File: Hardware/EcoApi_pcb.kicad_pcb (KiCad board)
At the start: 4 copper layers, 90.6 x 58 mm, 177 parts, among them IC1 PCF8563T_5,518, IC2 SIP32431DR3-T1GE3, IC3 SIP32431DR3-T1GE3, J1 UFL, J10 TILT, J12 POWER ON, J2 614105150721, J3 B2B-XH-A, J4 POWER ON, J5 DBG, J6 TRACE, J7 I2C INTERNAL, J8 B5B-XH-A__LF__SN_, J9 B8B-XH-A_LF__SN_, Q1 MMBT4403*, Q2 FDC638P, Q3 IRLML6244TRPBF, Q4 BSS138, Q5 BSS138, Q6 IRLML6244TRPBF, Q7 FDC638P, U1 TPL5010DDCR, U10 TPS63900DSKR, U13 STM32F411CEU6, U2 HX711, U4 MB85RC16PNF-G-JNE1, U5 RFM95W-868S2, U6 W25Q32JVSS, U7 24LC02B_SN, U8 TP4056, Y1 Crystal_Small, Y2 Crystal_Small, Y3 Crystal_GND24

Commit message: Fix drc error
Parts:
- added R58: 10K, Resistor_SMD:R_0603_1608Metric, B.Cu at (183.1, 84.0)
- F1, F2: footprint EcoApi_pcb:0603-F1608X100N -> EcoApi_pcb:FUSC1608X100N
- U10: footprint EcoApi_pcb:TPS63900DSKR -> EcoApi_pcb:SON50P250X250X80-11N-D
- moved C32 8.53 mm to (163.0, 74.2)
- moved R71 8.47 mm to (171.2, 74.1), turned to 180 degrees
- moved C34 1.32 mm to (189.3, 59.6), turned to 270 degrees
- moved R63 1.00 mm to (175.3, 74.1)
- moved C33 0.65 mm to (192.6, 58.6), turned to 0 degrees
- moved L2 0.61 mm to (162.4, 57.9)
- moved D7 0.58 mm to (181.8, 75.4), turned to 0 degrees
- moved C11 0.54 mm to (215.0, 47.7)
- moved L3 0.45 mm to (181.8, 60.1)
- moved C12 0.44 mm to (215.1, 49.4)
- moved C10 0.43 mm to (211.5, 49.4)
- moved R75 0.33 mm to (184.9, 60.2), turned to 90 degrees
- moved C42 0.32 mm to (180.2, 48.8)
- moved R74 0.32 mm to (186.1, 58.9)
- moved C36 0.20 mm to (186.2, 59.9)
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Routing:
- net NRST: track 75.0 -> 106.5 mm, vias 6 -> 4
- net GND: track 63.5 -> 77.3 mm, vias 47 -> 59
- net WDG_RELOAD: track 62.8 -> 74.8 mm
- net +3V3: track 325.6 -> 334.5 mm
- net WAKEUP: track 41.4 -> 47.3 mm
- net BOOT0: track 41.2 -> 46.5 mm
- net EN_AVBATT-BTN_TARE: track 49.5 -> 44.6 mm
- net +3V3_int: track 194.2 -> 190.3 mm
- net VBAT: track 259.8 -> 257.2 mm
- net Net-(C2-Pad1): track 6.23 -> 8.09 mm
- net Net-(R74-Pad2): track 5.56 -> 4.62 mm
- net Net-(C33-Pad1): track 11.0 -> 10.1 mm
- net WDG_ALARM: track 46.9 -> 46.1 mm
- net VREF+: track 4.20 -> 4.80 mm
- net Net-(L2-Pad2): track 2.67 -> 3.25 mm
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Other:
- board text added: "+"
- board text added: "3v3"
- board text added: "A+"
- board text added: "A-"
- board text added: "BOOT0 en LED info en TRACE en SCALE type (full - half) WDG delay 1 en WDG delay 2 en"
- board text added: "CHRG"
- board text added: "CK-GAIN"
- board text added: "CLK"
- board text added: "DIO"
- board text added: "DONE"
- board text added: "E+"
- board text added: "E-"
- board text added: "EcoApi V2.0 03/22"
- board text added: "GND"
- board text added: "INFO"
- board text added: "PWR en"
- board text added: "PWR on"
- board text added: "RESET"
- board text added: "RST"
- board text added: "RX"
- board text added: "SCL"
- board text added: "SD-ANA"
- board text added: "SDA"
- board text added: "SH"
- board text added: "TARE"
- board text added: "TX"
- board text added: "WS"

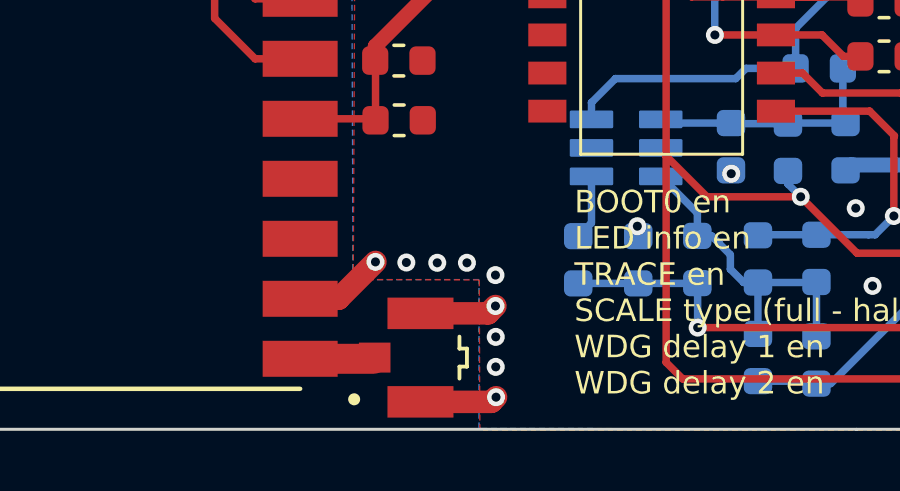
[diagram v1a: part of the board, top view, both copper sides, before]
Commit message: Add text on pcb front side
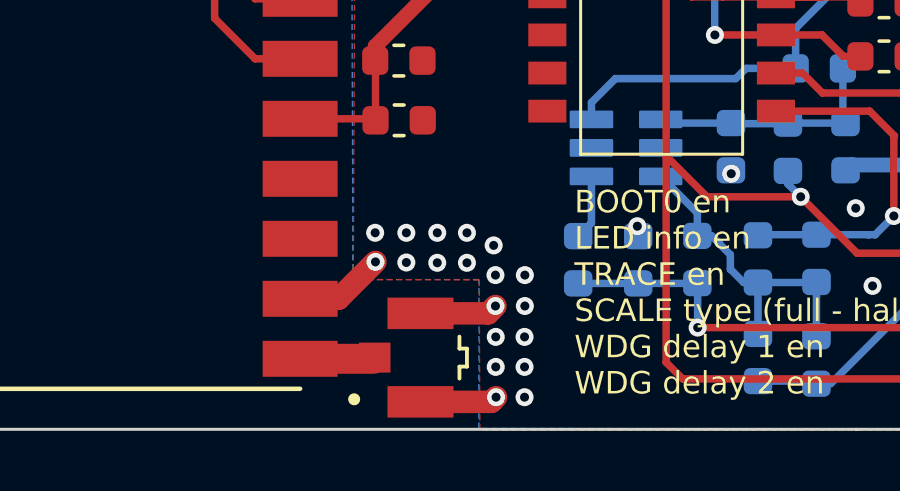
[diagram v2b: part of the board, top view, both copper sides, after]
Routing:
- net GND: vias 59 -> 69
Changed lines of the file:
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@@
     (thickness 1.6)
     (drawings 46)
-    (tracks 1760)
+    (tracks 1770)
     (zones 0)
     (modules 178)
@@
   )
   (setup
-    (last_trace_width 0.5)
+    (last_trace_width 0.25)
     (user_trace_width 0.4)
     (user_trace_width 0.5)
@@
   (gr_line (start 184.3 96) (end 220.6 96) (layer Edge.Cuts) (width 0.1))
   (gr_line (start 184.3 96) (end 148 96) (layer Edge.Cuts) (width 0.1))
-  (via (at 163.15 53.66) (size 0.6) (drill 0.3) (layers F.Cu B.Cu) (net 114))
-  (via (at 161.65 53.66) (size 0.6) (drill 0.3) (layers F.Cu B.Cu) (net 114))
-  (via (at 162.4 53.66) (size 0.6) (drill 0.3) (layers F.Cu B.Cu) (net 114))
   (segment (start 167.96 44.97) (end 167.96 40.6) (width 0.75) (layer F.Cu) (net 1))
   (segment (start 157.73 55.2) (end 167.96 44.97) (width 0.75) (layer F.Cu) (net 1))
@@
   (segment (start 205.94 52.23) (end 206.57 51.6) (width 0.5) (layer PWR) (net 113))
   (segment (start 205.94 53.19) (end 205.94 52.23) (width 0.5) (layer PWR) (net 113))
+  (via (at 163.15 53.66) (size 0.6) (drill 0.3) (layers F.Cu B.Cu) (net 114))
+  (via (at 161.65 53.66) (size 0.6) (drill 0.3) (layers F.Cu B.Cu) (net 114))
+  (via (at 162.4 53.66) (size 0.6) (drill 0.3) (layers F.Cu B.Cu) (net 114))
   (via (at 176.99 89.23) (size 0.6) (drill 0.3) (layers F.Cu B.Cu) (net 114))
   (via (at 180.12 87.48) (size 0.6) (drill 0.3) (layers F.Cu B.Cu) (net 114))
@@
   (via (at 181.65 77.1) (size 0.6) (drill 0.3) (layers F.Cu B.Cu) (net 114))
   (via (at 181.73 74.34) (size 0.6) (drill 0.3) (layers F.Cu B.Cu) (net 114))
+  (via (at 173.23 94.93) (size 0.6) (drill 0.3) (layers F.Cu B.Cu) (net 114))
+  (via (at 173.23 93.92) (size 0.6) (drill 0.3) (layers F.Cu B.Cu) (net 114))
+  (via (at 173.23 92.92) (size 0.6) (drill 0.3) (layers F.Cu B.Cu) (net 114))
+  (via (at 173.24 91.89) (size 0.6) (drill 0.3) (layers F.Cu B.Cu) (net 114))
+  (via (at 173.24 90.86) (size 0.6) (drill 0.3) (layers F.Cu B.Cu) (net 114))
+  (via (at 171.31 89.45) (size 0.6) (drill 0.3) (layers F.Cu B.Cu) (net 114))
+  (via (at 170.32 89.45) (size 0.6) (drill 0.3) (layers F.Cu B.Cu) (net 114))
+  (via (at 169.29 89.45) (size 0.6) (drill 0.3) (layers F.Cu B.Cu) (net 114))
+  (via (at 168.25 89.45) (size 0.6) (drill 0.3) (layers F.Cu B.Cu) (net 114))
+  (via (at 172.2 89.87) (size 0.6) (drill 0.3) (layers F.Cu B.Cu) (net 114))
   (zone (net 114) (net_name GND) (layer B.Cu) (hatch edge 0.508)
     (connect_pads yes (clearance 0.254))

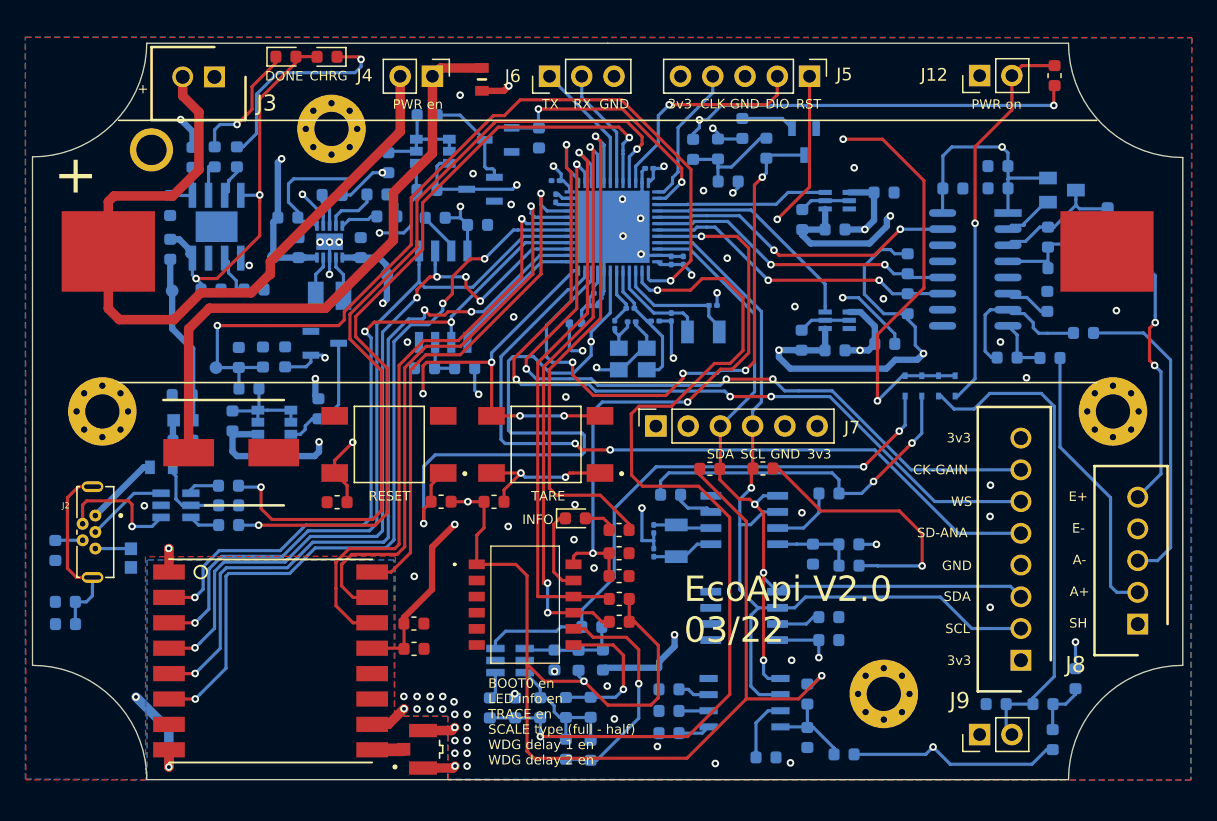
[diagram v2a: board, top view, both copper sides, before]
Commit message: Update pcb to v2.1 (Add ldo)
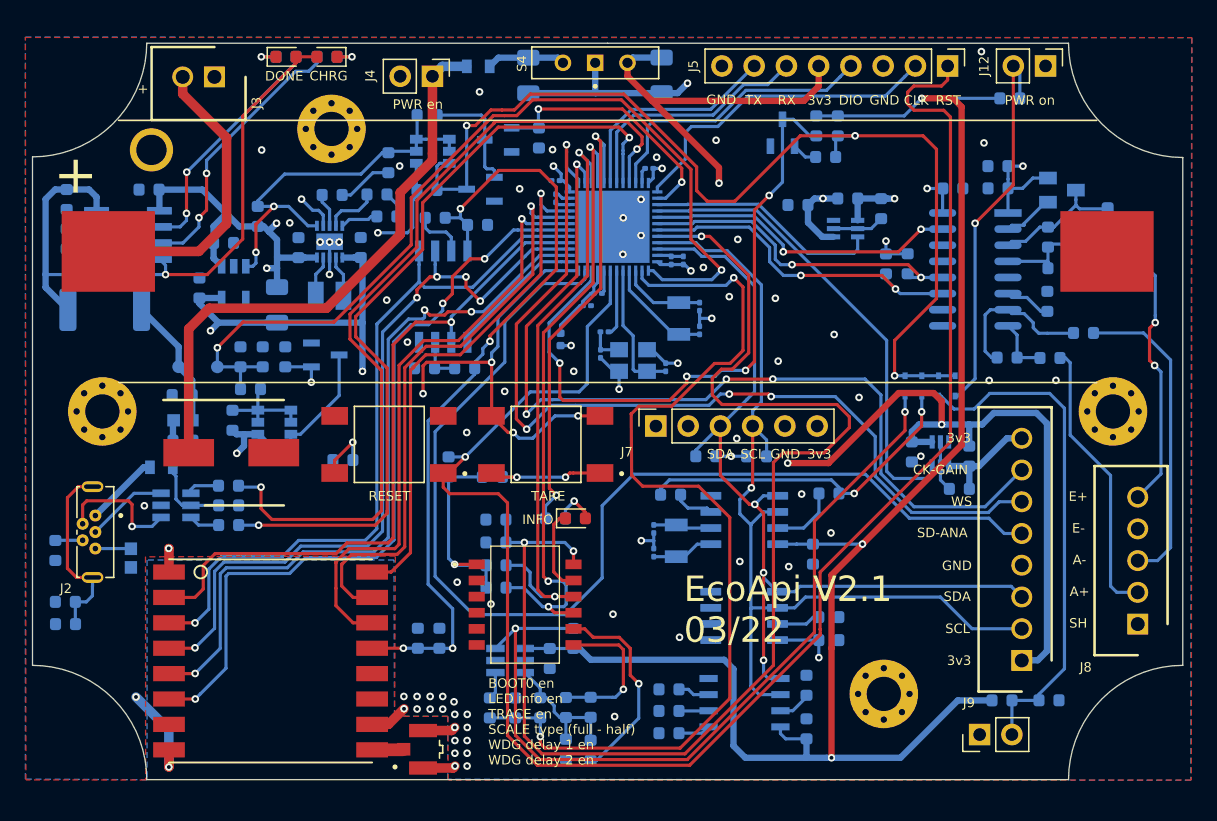
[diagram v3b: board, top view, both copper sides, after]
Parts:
- removed J6: TRACE, Connector_PinHeader_2.54mm:PinHeader_1x03_P2.54mm_Vertical
- removed R14, R43, R60, R64, R66: 0R, Resistor_SMD:R_0603_1608Metric
- removed R57: 100K, Resistor_SMD:R_0603_1608Metric
- removed R61, R62: 1M, Resistor_SMD:R_0603_1608Metric
- removed R74: 1M, Resistor_SMD:R_0201_0603Metric
- removed TP21, TP26, TP28: TestPoint, TestPoint:TestPoint_Pad_D1.0mm
- added C45: 1uF, Capacitor_SMD:C_0603_1608Metric, B.Cu at (152.2, 57.3)
- added C46: 10nF, Capacitor_SMD:C_0603_1608Metric, B.Cu at (157.1, 62.7)
- added PS1: NCP161ASN330T1G, EcoApi_pcb:SOT95P280X145-5N, B.Cu at (154.8, 56.8)
- added S4: MSS-102559-14A-D, EcoApi_pcb:SW_MSS-102559-14A-D, F.Cu at (183.3, 39.5)
- added TP3: TestPoint, TestPoint:TestPoint_Pad_D1.0mm, B.Cu at (153.6, 63.5)
- C10: value 0.1uF 0402 6.3V -> 0.1uF
- C11: value 0.1uF 0402 -> 0.1uF
- C12: value 10uF 0402 -> 10uF
- C13, C14, C15: value 100n -> 0.1uF
- C18: value EEE-FK0J102GP -> 1000uF
- C22, C30: value 100nF -> 0.1uF
- C23: value 10uF 6.3V X5R -> 10uF
- C24: value 22uF 6.3V x5R -> 22uF
- C26, C28: value 1u -> 1uF
- C27: value 0.01uF -> 1uF
- C29, C44: value 0.1u -> 0.1uF
- C31, C32: value 100nF -> 0.1uF; moved to B.Cu
- C35, C36: value 10u -> 10uF
- C4: value 10uF 0402 6.3V -> 10uF
- C5, C6, C7: value 100nF 0402 -> 0.1uF
- C8: value 100n -> 0.1uF; moved to B.Cu
- C9: value 10u -> 10uF; moved to B.Cu
- D1: value LED_0603_RED -> RED
- D2: value LED_0603_GREEN -> GREEN
- D7: value LED_0603_BLUE -> BLUE
- F2, R63, R72: moved to B.Cu
- J5: value DBG -> Debug; footprint Connector_PinHeader_2.54mm:PinHeader_1x05_P2.54mm_Vertical -> Connector_PinHeader_2.54mm:PinHeader_1x08_P2.54mm_Vertical
- L1, L3: value 3.3uH_0603 -> 3.3uH
- L2: value DFE252012P-2R2M=P2 -> 2.2uH
- Q1: value MMBT4403* -> MMBT4403
- R10, R46: footprint Resistor_SMD:R_0603_1608Metric -> Resistor_SMD:R_1206_3216Metric
- R15, R42, R45: value 0R -> 1M
- R21: value 22k -> 22K
- R22: value 20k -> 20K
- R23: value 0R -> 100K
- R26, R28: value 4.7k -> 4.7K; moved to B.Cu
- R29, R32: value 4.7k -> 4.7K
- R35: value 0.5R_2W_2512 -> 0.5R; footprint Resistor_SMD:R_0603_1608Metric -> Resistor_SMD:R_2512_6332Metric
- R52: value 36k5 -> 36.5K
- R56: value 1M -> 0R; footprint Resistor_SMD:R_0603_1608Metric -> Resistor_SMD:R_1206_3216Metric
- R67, R68, R69, R71, R73: value 10k -> 10K; moved to B.Cu
- U4: value MB85RC16PNF-G-JNE1 -> MB85RC04VPNF-G-JNERE1
- U7: value 24LC02B_SN -> 24LC02BT-I/SN
- moved R11 54.1 mm to (156.7, 51.6), turned to 270 degrees
- moved R23 54.0 mm to (158.9, 62.7), turned to 90 degrees
- moved R25 50.2 mm to (154.8, 67.7), turned to 90 degrees
- moved R10 48.8 mm to (158.3, 58.6), turned to 270 degrees
- moved R45 40.8 mm to (155.4, 62.7), turned to 90 degrees
- moved R56 37.7 mm to (188.6, 40.5)
- moved R15 28.5 mm to (158.6, 70.3), turned to 0 degrees
- moved C44 24.6 mm to (212.0, 73.1), turned to 180 degrees
- moved IC3 21.5 mm to (210.5, 70.3), turned to 90 degrees
- moved R13 20.7 mm to (212.8, 70.5), turned to 270 degrees
- moved C28 20.5 mm to (208.3, 70.2), turned to 270 degrees
- moved R42 18.8 mm to (156.2, 65.2), turned to 180 degrees
- moved R39 15.3 mm to (141.7, 53.4), turned to 270 degrees
- moved R46 14.2 mm to (178.1, 40.5)
- moved C16 13.4 mm to (141.7, 50.3), turned to 270 degrees
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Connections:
- C13 pad 2: Net-(C13-Pad2) -> V_WKUP
- C2 pad 1: Net-(C2-Pad1) -> V_WKUP
- C21 pad 1: Net-(C21-Pad1) -> VBATT
- C23 pad 1: VBAT -> VBATT
- C25 pad 1: Net-(C25-Pad1) -> V_WKUP
- C27 pad 1: ANA_VBATT -> VBATT
- F2 pad 2: VBAT -> VBATT
- IC1 pad 8: Net-(C25-Pad1) -> V_WKUP
- J5 pad 2: SW_DIO -> SW_CLK
- J5 pad 4: SW_CLK -> SW_DIO
- Q2 pad 4: VBAT -> VBATT
- Q7 pad 4: VBAT -> VBATT
- R10 pad 1: VBAT -> VBATT
- R10 pad 2: Net-(C25-Pad1) -> +3V3
- R11 pad 1: +3V3 -> EN_3V3
- R11 pad 2: Net-(C25-Pad1) -> VBATT
- R15 pad 1: +3V3 -> VBATT
- R15 pad 2: Net-(C2-Pad1) -> Net-(Q6-Pad3)
- R23 pad 1: VBAT -> EN_AVBATT-BTN_TARE
- R23 pad 2: Net-(C13-Pad2) -> GND
- R25 pad 1: +3V3 -> VBATT
- R25 pad 2: Net-(C13-Pad2) -> Net-(Q7-Pad1)
- R42 pad 1: VBAT -> Net-(Q7-Pad1)
- R42 pad 2: Net-(C21-Pad1) -> ANA_VBATT
- R44 pad 1: VBAT -> VBATT
- R45 pad 1: +3V3 -> ANA_VBATT
- R45 pad 2: Net-(R45-Pad2) -> GND
- R46 pad 1: VBAT -> VBATT
- R46 pad 2: Net-(R45-Pad2) -> V_WKUP
- R47 pad 1: Net-(R45-Pad2) -> V_WKUP
- R51 pad 1: Net-(R45-Pad2) -> V_WKUP
- R56 pad 1: VBAT -> +3V3
- R56 pad 2: Net-(Q6-Pad3) -> V_WKUP
- R58 pad 2: Net-(C2-Pad1) -> V_WKUP
- R65 pad 1: Net-(R64-Pad2) -> V_WKUP
- R73 pad 1: VBAT -> V_WKUP
- U1 pad 1: Net-(C2-Pad1) -> V_WKUP
- U10 pad 10: VBAT -> VBATT
- U10 pad 2: VBAT -> VBATT
- U13 pad 39: EN_3V3_EXT -> EN_3V3_INT
- U13 pad 40: EN_3V3_INT -> EN_3V3_EXT
- U4 pad 8: Net-(C13-Pad2) -> V_WKUP
- U8 pad 5: Net-(C21-Pad1) -> VBATT
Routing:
- net VBAT: track 257.2 -> 0.00 mm, vias 12 -> 0
- net +3V3: track 334.5 -> 142.9 mm, vias 13 -> 12
- net V_WKUP: track 0.00 -> 146.0 mm, vias 0 -> 4
- net +3V3_int: track 190.3 -> 85.3 mm, vias 7 -> 9
- net BOOT0: track 46.5 -> 101.8 mm
- net VBATT: track 0.00 -> 49.3 mm, vias 0 -> 5
- net NRST: track 106.5 -> 148.3 mm, vias 4 -> 2
- net +3V3_EXT: track 36.7 -> 8.46 mm, vias 1 -> 0
- net I2S_SD-MIC_ANA: track 60.3 -> 88.0 mm, vias 2 -> 0
- net GND: track 77.3 -> 52.1 mm, vias 69 -> 70
- net EN_3V3_EXT: track 13.6 -> 37.3 mm
- net Net-(C16-Pad1): track 30.3 -> 51.0 mm, vias 2 -> 1
- net WDG_ALARM: track 46.1 -> 65.3 mm
- net Net-(R36-Pad1): track 2.65 -> 21.5 mm, vias 0 -> 2
- net Net-(R37-Pad1): track 2.72 -> 18.8 mm, vias 0 -> 2
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- added copper zone on PWR, net +3V3
- added copper zone on PWR, net +3V3_int
- added copper zone on PWR, net VBATT
- added copper zone on PWR, net V_WKUP
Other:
- board text added: "EcoApi V2.1 03/22"
- board text removed: "EcoApi V2.0 03/22"

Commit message: Add Gerber files, Bom, Jlcpcb LCSC parts ref, some optimizations
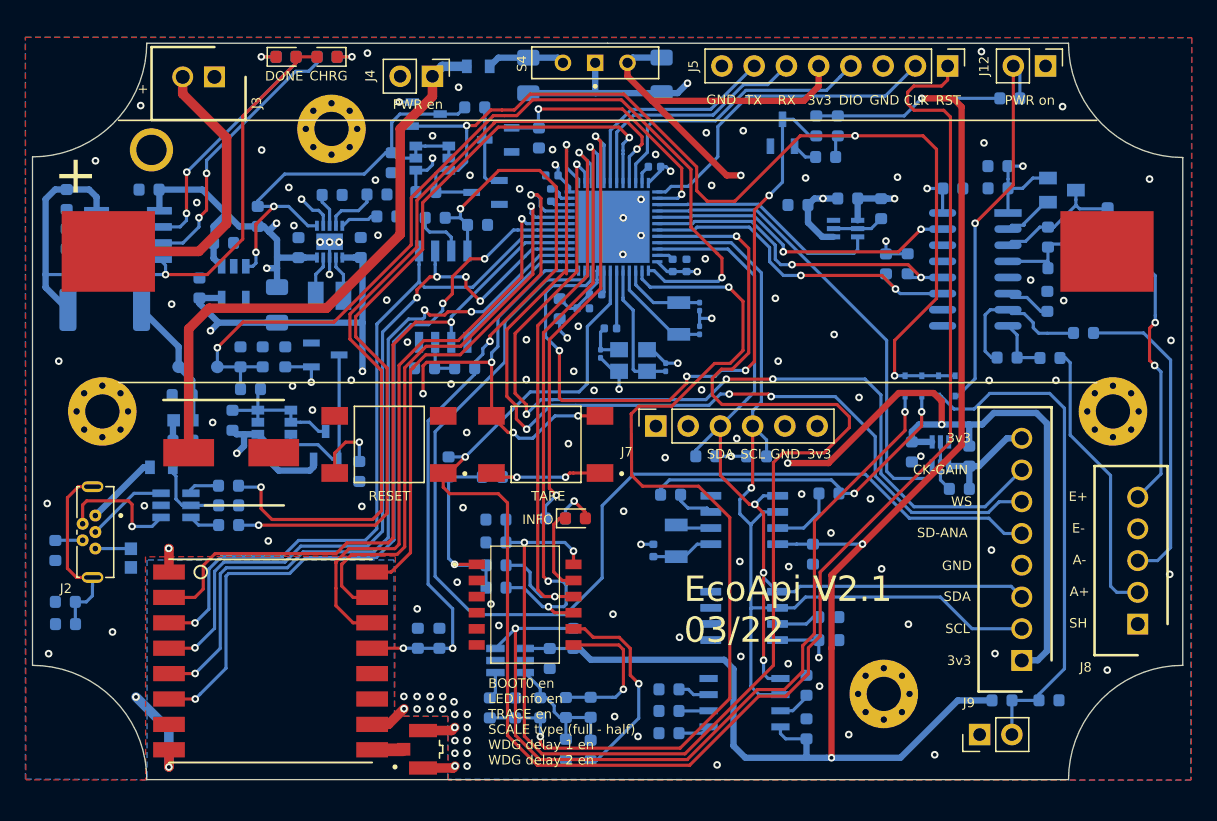
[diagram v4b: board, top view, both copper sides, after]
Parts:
- removed C3: 22pF, Capacitor_SMD:C_0201_0603Metric
- added Q8: BSS84AK,215, EcoApi_pcb:SOT95P230X110-3N, B.Cu at (170.0, 43.6)
- added Q9: BSS84AK,215, EcoApi_pcb:SOT95P230X110-3N, B.Cu at (162.1, 69.7)
- C1, C37, C38, C39, C40, C41, C42, C43: footprint Capacitor_SMD:C_0201_0603Metric -> Capacitor_SMD:C_0402_1005Metric
- C25: value 10uF -> 0.1uF
- C33, C34: value 1.5pF -> 6pF
- C35, C36: value 10uF -> 8pF
- L3: value 3.3uH -> 600Ω@100MHz; footprint Inductor_SMD:L_0402_1005Metric -> Inductor_SMD:L_0603_1608Metric
- R75: value ?k -> 787R; footprint Resistor_SMD:R_0201_0603Metric -> Resistor_SMD:R_0402_1005Metric
- U8: value TP4056 -> TP4056M
- Y1: value Crystal_Small -> 32.768kHz 12.5pF
- Y2: value Crystal_Small -> 32.768kHz 6pF
- Y3: value Crystal_GND24 -> 25mHz 9pF +-10ppm
- moved R48 3.80 mm to (173.8, 43.0)
- moved L3 2.42 mm to (180.5, 58.9)
- moved C32 1.57 mm to (164.7, 71.7), turned to 270 degrees
- moved R75 0.54 mm to (184.5, 60.5)
- moved Q2 0.54 mm to (170.5, 47.0)
- moved C42 0.50 mm to (179.9, 48.4)
- moved Q3 0.47 mm to (174.7, 49.8)
- moved C40 0.46 mm to (190.5, 55.5)
- moved C39 0.45 mm to (179.8, 50.0)
- moved C43 0.44 mm to (188.0, 47.7)
- moved C41 0.41 mm to (189.4, 55.5)
- moved C38 0.36 mm to (182.4, 58.9)
- moved R53 0.26 mm to (167.3, 47.4)
- moved C37 0.20 mm to (183.3, 57.8)
- moved R44 0.18 mm to (170.0, 49.7)
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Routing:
- net GND: track 52.1 -> 44.7 mm, vias 70 -> 120
- net EN_3V3: track 32.2 -> 39.0 mm
- net Net-(Q6-Pad3): track 9.81 -> 14.0 mm
- net PWR_ON: track 82.8 -> 86.8 mm
- net Net-(Q7-Pad1): track 8.25 -> 11.3 mm
- net +3V3: track 142.9 -> 145.7 mm, vias 12 -> 13
- net Net-(Q3-Pad1): track 9.08 -> 6.77 mm
- net WAKEUP: track 51.9 -> 53.8 mm
- net Net-(IC1-Pad2): track 4.60 -> 2.83 mm
- net VBATT: track 49.3 -> 51.0 mm, vias 5 -> 6
- net NRST: track 148.3 -> 150.0 mm
- net WDG_ALARM: track 65.3 -> 66.5 mm
- net BOOT0: track 101.8 -> 103.1 mm
- net WDG_RELOAD: track 76.1 -> 75.0 mm
- net LORA_DIO2: track 41.2 -> 42.3 mm
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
